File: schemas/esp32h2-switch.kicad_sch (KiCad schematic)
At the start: 21 parts, among them J1 Screw_Terminal_01x02, J2 Screw_Terminal_01x02, J3 Conn_01x15, J4 Conn_01x15, K1 SPDT, 5V 72R, 10A 250VAC, Q1 NPN, 40V, 500mA, U1 LM1117MP-3.3

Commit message: Fix nets due to checks
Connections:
- net L: no longer F1.1, J1.1 (Pin_1), J2.1 (Pin_1), K1.11, K1.14
- new net L_IN: F1.1, J1.1 (Pin_1), K1.11
- new net L_OUT: J2.1 (Pin_1), K1.14
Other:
- moved on the sheet: F1, J2, RV1
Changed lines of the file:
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@@
 	)
 	(junction
+		(at 86.36 71.12)
+		(diameter 0)
+		(color 0 0 0 0)
+	)
+	(junction
 		(at 87.63 118.11)
 		(diameter 0)
@@
 	)
 	(junction
-		(at 83.82 78.74)
+		(at 86.36 78.74)
 		(diameter 0)
 		(color 0 0 0 0)
@@
 	)
 	(junction
-		(at 83.82 71.12)
-		(diameter 0)
-		(color 0 0 0 0)
-	)
-	(junction
 		(at 99.06 118.11)
 		(diameter 0)
@@
 	(wire
 		(pts
-			(xy 99.06 118.11) (xy 114.3 118.11)
+			(xy 86.36 71.12) (xy 99.06 71.12)
 		)
 		(stroke
@@
 	(wire
 		(pts
-			(xy 83.82 71.12) (xy 99.06 71.12)
+			(xy 99.06 118.11) (xy 114.3 118.11)
 		)
 		(stroke
@@
 	(wire
 		(pts
-			(xy 68.58 71.12) (xy 72.39 71.12)
+			(xy 73.66 71.12) (xy 74.93 71.12)
 		)
 		(stroke
@@
 	(wire
 		(pts
-			(xy 182.88 128.27) (xy 186.69 128.27)
-		)
-		(stroke
-			(width 0)
-			(type default)
-		)
-	)
-	(wire
-		(pts
 			(xy 196.85 95.25) (xy 196.85 105.41)
 		)
@@
 	(wire
 		(pts
+			(xy 86.36 78.74) (xy 99.06 78.74)
+		)
+		(stroke
+			(width 0)
+			(type default)
+		)
+	)
+	(wire
+		(pts
 			(xy 72.39 118.11) (xy 87.63 118.11)
 		)
@@
 	(wire
 		(pts
-			(xy 80.01 71.12) (xy 83.82 71.12)
+			(xy 182.88 128.27) (xy 190.5 128.27)
+		)
+		(stroke
+			(width 0)
+			(type default)
+		)
+	)
+	(wire
+		(pts
+			(xy 82.55 71.12) (xy 86.36 71.12)
 		)
 		(stroke
@@
 	(wire
 		(pts
-			(xy 157.48 134.62) (xy 186.69 134.62)
+			(xy 157.48 134.62) (xy 190.5 134.62)
 		)
 		(stroke
@@
 	(wire
 		(pts
-			(xy 186.69 130.81) (xy 186.69 134.62)
+			(xy 190.5 130.81) (xy 190.5 134.62)
 		)
 		(stroke
@@
 	(wire
 		(pts
-			(xy 68.58 78.74) (xy 83.82 78.74)
+			(xy 73.66 78.74) (xy 86.36 78.74)
 		)
 		(stroke
@@
 	(wire
 		(pts
-			(xy 83.82 78.74) (xy 99.06 78.74)
-		)
-		(stroke
-			(width 0)
-			(type default)
-		)
-	)
-	(wire
-		(pts
 			(xy 99.06 118.11) (xy 99.06 116.84)
 		)
@@
 		)
 	)
-	(label "L"
-		(at 184.15 128.27 0)
+	(label "RELAY_COIL"
+		(at 184.15 115.57 0)
 		(effects
 			(font
@@
 		)
 	)
-	(label "RELAY_COIL"
-		(at 184.15 115.57 0)
+	(label "RELAY_CTRL"
+		(at 193.04 72.39 180)
 		(effects
 			(font
 				(size 1.27 1.27)
 			)
-			(justify left bottom)
+			(justify right bottom)
 		)
 	)
-	(label "RELAY_CTRL"
-		(at 193.04 72.39 180)
+	(label "L_OUT"
+		(at 184.15 128.27 0)
 		(effects
 			(font
 				(size 1.27 1.27)
 			)
-			(justify right bottom)
+			(justify left bottom)
 		)
 	)
 	(label "L"
-		(at 86.36 71.12 0)
+		(at 95.25 71.12 0)
 		(effects
 			(font
@@
 		(lib_name "Screw_Terminal_01x02_1")
 		(lib_id "Connector:Screw_Terminal_01x02")
-		(at 191.77 128.27 0)
+		(at 195.58 128.27 0)
 		(unit 1)
 		(exclude_from_sim no)
@@
 		(dnp no)
 		(property "Reference" "J2"
-			(at 191.77 133.604 0)
+			(at 195.58 133.604 0)
 			(effects
 				(font
@@
 		)
 		(property "Value" "Screw_Terminal_01x02"
-			(at 191.77 134.62 0)
+			(at 195.58 134.62 0)
 			(effects
 				(font
@@
 		)
 		(property "Footprint" "TerminalBlock_Phoenix:TerminalBlock_Phoenix_MKDS-1,5-2-5.08_1x02_P5.08mm_Horizontal"
-			(at 191.77 128.27 0)
+			(at 195.58 128.27 0)
 			(effects
 				(font
@@
 		)
 		(property "Datasheet" "~"
-			(at 191.77 128.27 0)
+			(at 195.58 128.27 0)
 			(effects
 				(font
@@
 		)
 		(property "Description" "Generic screw terminal, single row, 01x02, script generated (kicad-library-utils/schlib/autogen/connector/)"
-			(at 191.77 128.27 0)
+			(at 195.58 128.27 0)
 			(effects
 				(font
@@
 		(on_board yes)
 		(dnp no)
-		(fields_autoplaced yes)
 		(property "Reference" "#PWR012"
 			(at 161.29 125.73 0)
@@
 			)
 		)
-		(property "Value" "L"
-			(at 153.67 125.7299 90)
+		(property "Value" "L_IN"
+			(at 151.638 125.73 90)
 			(effects
 				(font
 					(size 1.27 1.27)
 				)
-				(justify left)
 			)
 		)
@@
 		(lib_name "Varistor_1")
 		(lib_id "Device:Varistor")
-		(at 83.82 74.93 0)
+		(at 86.36 74.93 0)
 		(unit 1)
 		(exclude_from_sim no)
@@
 		(fields_autoplaced yes)
 		(property "Reference" "RV1"
-			(at 86.36 73.8532 0)
+			(at 88.9 73.8532 0)
 			(effects
 				(font
@@
 		)
 		(property "Value" "275V"
-			(at 86.36 76.3932 0)
+			(at 88.9 76.3932 0)
 			(effects
 				(font
@@
 		)
 		(property "Footprint" "Varistor:RV_Disc_D9mm_W3.4mm_P5mm"
-			(at 82.042 74.93 90)
+			(at 84.582 74.93 90)
 			(effects
 				(font
@@
 		)
 		(property "Datasheet" "~"
-			(at 83.82 74.93 0)
+			(at 86.36 74.93 0)
 			(effects
 				(font
@@
 		)
 		(property "Description" "Voltage dependent resistor"
-			(at 83.82 74.93 0)
+			(at 86.36 74.93 0)
 			(effects
 				(font
@@
 		)
 		(property "Sim.Name" "kicad_builtin_varistor"
-			(at 83.82 74.93 0)
+			(at 86.36 74.93 0)
 			(effects
 				(font
@@
 		)
 		(property "Sim.Device" "SUBCKT"
-			(at 83.82 74.93 0)
+			(at 86.36 74.93 0)
 			(effects
 				(font
@@
 		)
 		(property "Sim.Pins" "1=A 2=B"
-			(at 83.82 74.93 0)
+			(at 86.36 74.93 0)
 			(effects
 				(font
@@
 		)
 		(property "Sim.Params" "threshold=1k"
-			(at 83.82 74.93 0)
+			(at 86.36 74.93 0)
 			(effects
 				(font
@@
 		)
 		(property "Sim.Library" "${KICAD9_SYMBOL_DIR}/Simulation_SPICE.sp"
-			(at 83.82 74.93 0)
+			(at 86.36 74.93 0)
 			(effects
 				(font
@@
 	(symbol
 		(lib_id "Device:Fuse")
-		(at 76.2 71.12 90)
+		(at 78.74 71.12 90)
 		(unit 1)
 		(exclude_from_sim no)
@@
 		(fields_autoplaced yes)
 		(property "Reference" "F1"
-			(at 76.2 64.77 90)
+			(at 78.74 64.77 90)
 			(effects
 				(font
@@
 		)
 		(property "Value" "T250mA 250V"
-			(at 76.2 67.31 90)
+			(at 78.74 67.31 90)
 			(effects
 				(font
@@
 		)
 		(property "Footprint" "Sivakov_FuseHolders_THT:FuseHolder_THT_5x20mm_PTF76_RM15mm"
-			(at 76.2 72.898 90)
+			(at 78.74 72.898 90)
 			(effects
 				(font
@@
 		)
 		(property "Datasheet" "~"
-			(at 76.2 71.12 0)
+			(at 78.74 71.12 0)
 			(effects
 				(font
@@
 		)
 		(property "Description" "Fuse"
-			(at 76.2 71.12 0)
+			(at 78.74 71.12 0)
 			(effects
 				(font
@@
 			)
 		)
-		(property "Value" "L"
+		(property "Value" "L_IN"
 			(at 59.69 71.1199 90)
 			(effects
@@
 	(symbol
 		(lib_id "power:+5V")
-		(at 68.58 78.74 90)
+		(at 73.66 78.74 90)
 		(unit 1)
 		(exclude_from_sim no)
@@
 		(fields_autoplaced yes)
 		(property "Reference" "#PWR06"
-			(at 72.39 78.74 0)
+			(at 77.47 78.74 0)
 			(effects
 				(font
@@
 		)
 		(property "Value" "N"
-			(at 64.77 78.7399 90)
+			(at 69.85 78.7399 90)
 			(effects
 				(font
@@
 		)
 		(property "Footprint" ""
-			(at 68.58 78.74 0)
+			(at 73.66 78.74 0)
 			(effects
 				(font
@@
 		)
 		(property "Datasheet" ""
-			(at 68.58 78.74 0)
+			(at 73.66 78.74 0)
 			(effects
 				(font
@@
 		)
 		(property "Description" "Power symbol creates a global label with name \"+5V\""
-			(at 68.58 78.74 0)
+			(at 73.66 78.74 0)
 			(effects
 				(font
@@
 	(symbol
 		(lib_id "power:+5V")
-		(at 68.58 71.12 90)
+		(at 73.66 71.12 90)
 		(unit 1)
 		(exclude_from_sim no)
@@
 		(on_board yes)
 		(dnp no)
-		(fields_autoplaced yes)
 		(property "Reference" "#PWR05"
-			(at 72.39 71.12 0)
+			(at 77.47 71.12 0)
 			(effects
 				(font
@@
 			)
 		)
-		(property "Value" "L"
-			(at 64.77 71.1199 90)
+		(property "Value" "L_IN"
+			(at 67.818 71.12 90)
 			(effects
 				(font
 					(size 1.27 1.27)
 				)
-				(justify left)
 			)
 		)
 		(property "Footprint" ""
-			(at 68.58 71.12 0)
+			(at 73.66 71.12 0)
 			(effects
 				(font
@@
 		)
 		(property "Datasheet" ""
-			(at 68.58 71.12 0)
+			(at 73.66 71.12 0)
 			(effects
 				(font
@@
 		)
 		(property "Description" "Power symbol creates a global label with name \"+5V\""
-			(at 68.58 71.12 0)
+			(at 73.66 71.12 0)
 			(effects
 				(font

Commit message: Better layout for hand soldering
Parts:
- Q1: footprint Package_TO_SOT_THT:TO-92_Inline -> Package_TO_SOT_THT:TO-92_Inline_Wide
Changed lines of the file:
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@@
 			)
 		)
-		(property "Footprint" "Package_TO_SOT_THT:TO-92_Inline"
+		(property "Footprint" "Package_TO_SOT_THT:TO-92_Inline_Wide"
 			(at 231.14 118.11 0)
 			(effects

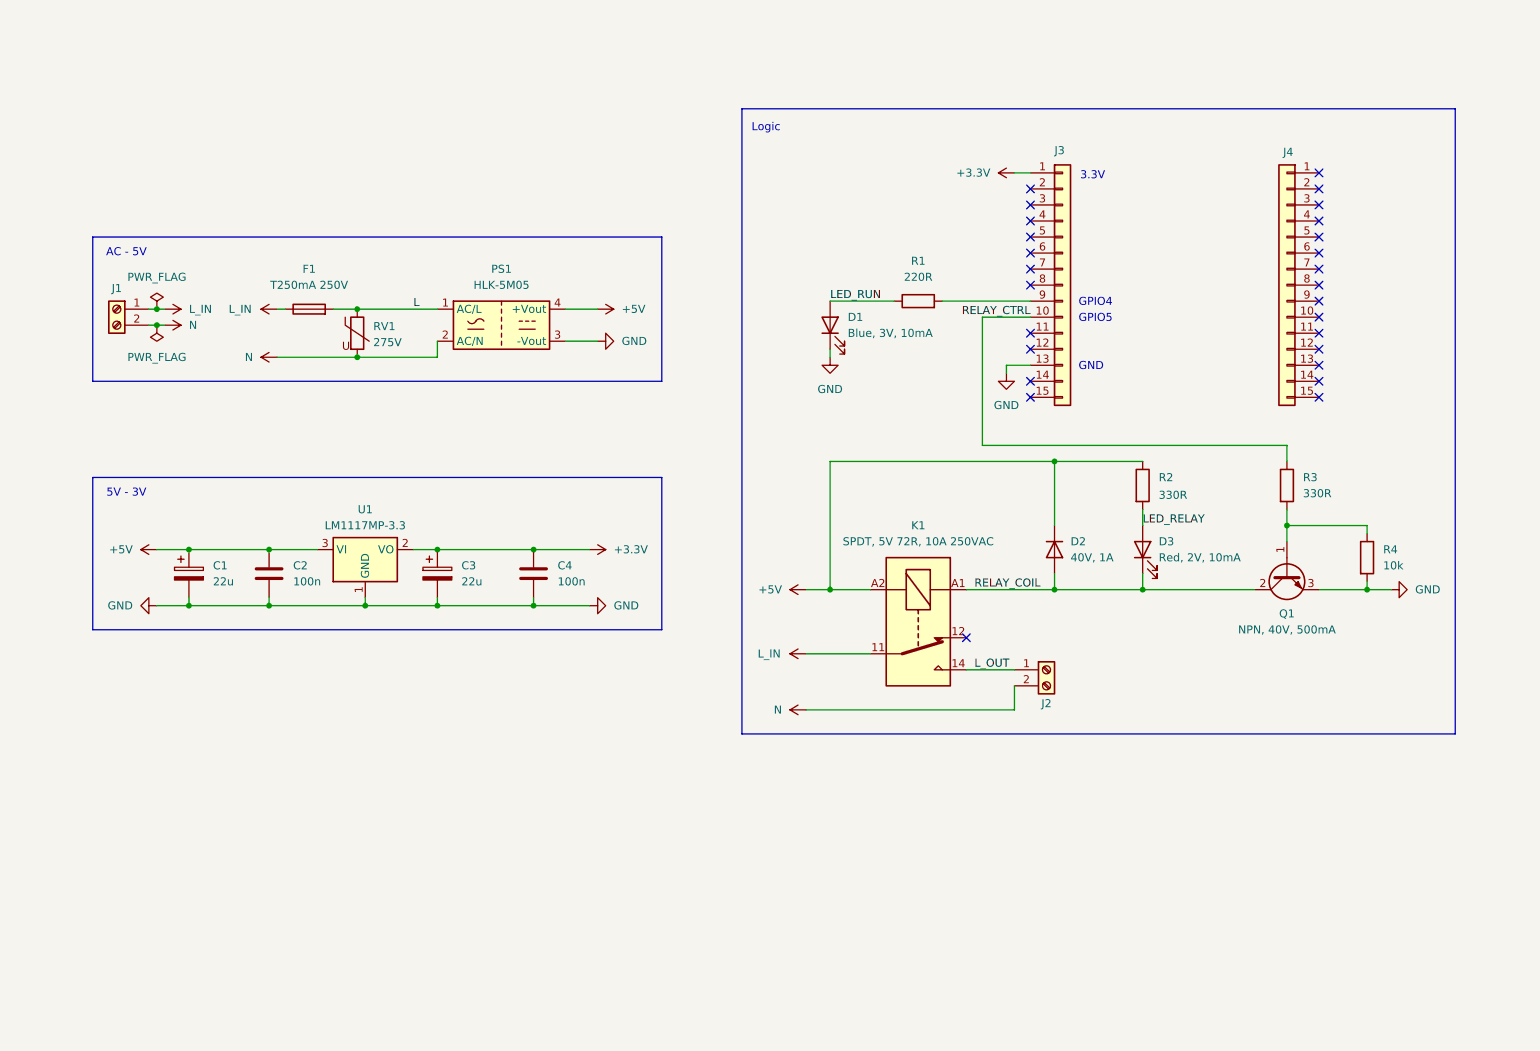
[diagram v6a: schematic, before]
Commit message: Fix footprints and improve layout for hand soldering
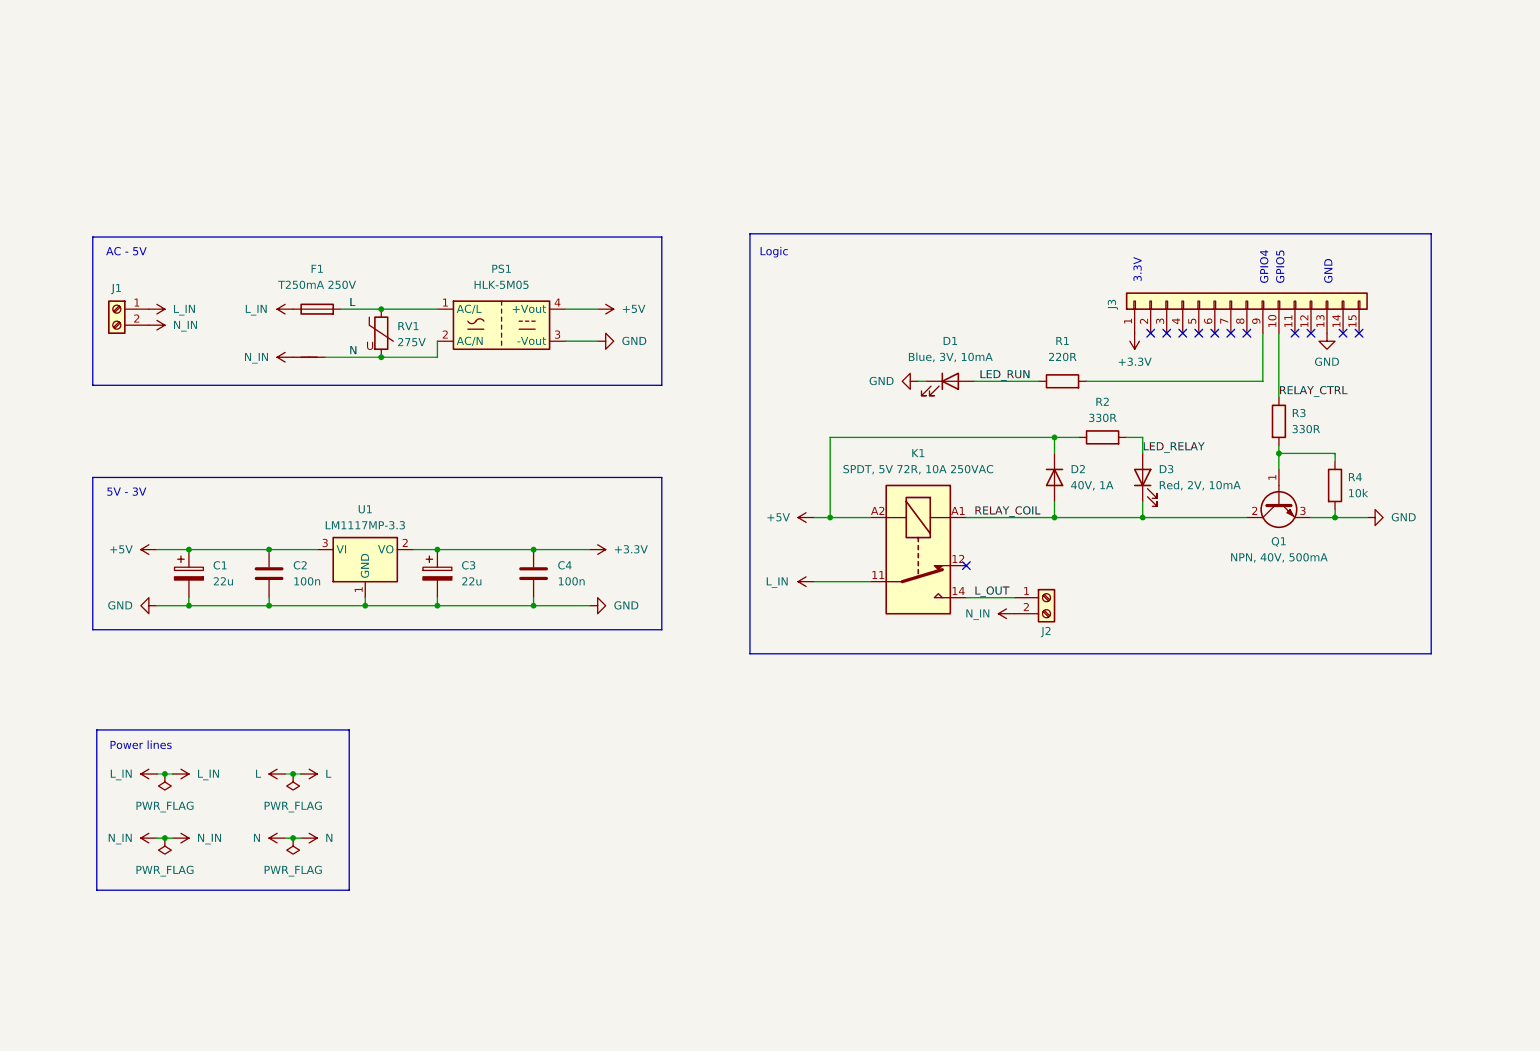
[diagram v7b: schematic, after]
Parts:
- removed J4: Conn_01x15, Connector_PinSocket_2.54mm:PinSocket_1x15_P2.54mm_Vertical, symbol Connector_Generic:Conn_01x15
- added NT1: NetTie_2, NetTie:NetTie-2_SMD_Pad2.0mm, symbol Device:NetTie_2
- C1, C3: footprint Sivakov_Capacitors_THT:CP_Radial_D5.0mm_P1.50mm -> KiCadX_Capacitors_THT:CP_Radial_D5.0mm_P1.50mm
- F1: footprint Sivakov_FuseHolders_THT:FuseHolder_THT_5x20mm_PTF76_RM15mm -> KiCadX_FuseHolders_THT:FuseHolder_THT_5x20mm_PTF76_RM15mm
- K1: footprint Sivakov_Relays_THT:Relay_SPDT_Relpol-RM51 -> KiCadX_Relays_THT:Relay_SPDT_Relpol-RM51
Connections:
- net N: now also NT1.2; no longer J1.2 (Pin_2), J2.2 (Pin_2)
- new net N_IN: J1.2 (Pin_2), J2.2 (Pin_2), NT1.1
- no-connect marks 27 -> 12
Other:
- note added: "Power lines"
- moved on the sheet: D1, D2, D3, F1, J2, J3, K1, Q1, R1, R3, R4, RV1

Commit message: Replace HLK block with SMPS
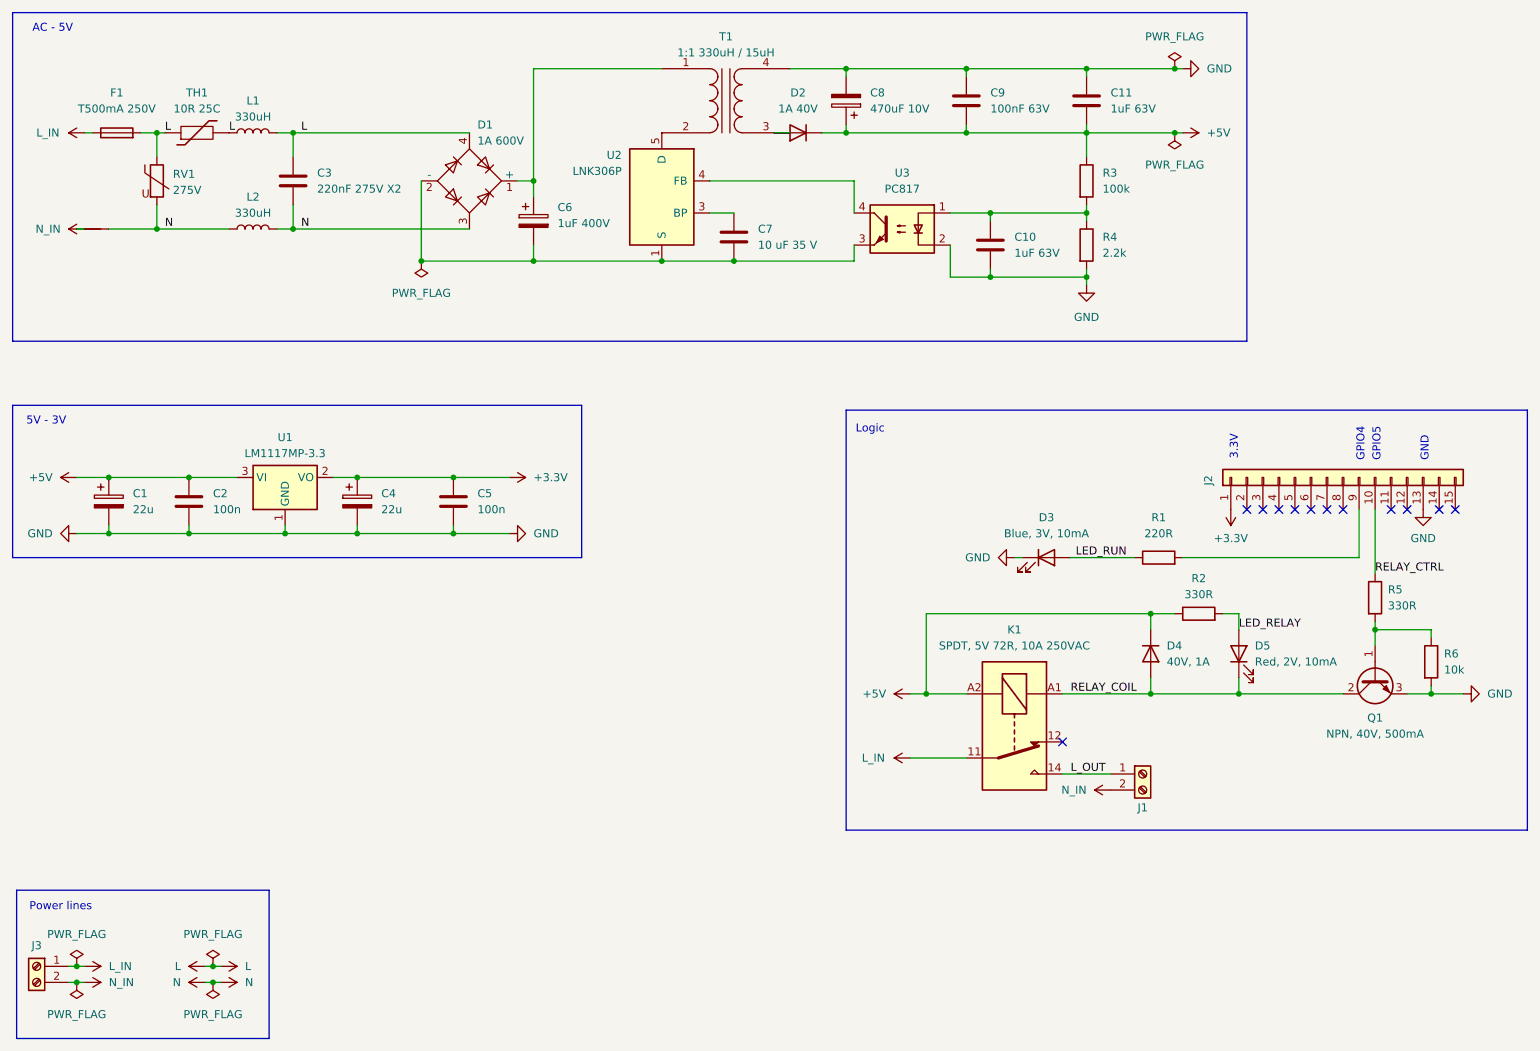
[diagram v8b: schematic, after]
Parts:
- removed J1: Screw_Terminal_01x02, TerminalBlock_Phoenix:TerminalBlock_Phoenix_MKDS-1,5-2-5.08_1x02_P5.08mm_Horizontal, symbol Connector:Screw_Terminal_01x02
- removed PS1: HLK-5M05, Converter_ACDC:Converter_ACDC_Hi-Link_HLK-5Mxx, symbol Converter_ACDC:HLK-5M05
- added C10, C11: 1uF 63V, symbol Device:C
- added C3: 220nF 275V X2, symbol Device:C
- added C6: 1uF 400V, symbol Device:C_Polarized
- added C7: 10 uF 35 V, symbol Device:C
- added C8: 470uF 10V, symbol Device:C_Polarized
- added C9: 100nF 63V, symbol Device:C
- added D1: 1A 600V, Diode_THT:Diode_Bridge_DIP-4_W7.62mm_P5.08mm, symbol Diode_Bridge:DF08M
- added D2: 1A 40V, symbol Device:D
- added J3: Screw_Terminal_01x02, TerminalBlock_Phoenix:TerminalBlock_Phoenix_MKDS-1,5-2-5.08_1x02_P5.08mm_Horizontal, symbol Connector:Screw_Terminal_01x02
- added L1, L2: 330uH, symbol Device:L
- added R3: 100k, symbol Device:R
- added R4: 2.2k, symbol Device:R
- added T1: 1:1 330uH / 15uH, symbol Device:Transformer_1P_1S
- added TH1: 10R 25C, symbol Device:Thermistor
- added U2: LNK306P, Package_DIP:PowerIntegrations_PDIP-8B, symbol Regulator_Switching:LNK306P
- added U3: PC817, Package_DIP:DIP-4_W7.62mm, symbol Isolator:PC817
- F1: value T250mA 250V -> T500mA 250V
- renumbered C3 to C4, C4 to C5, D1 to D3, D2 to D4, D3 to D5, J2 to J1, J3 to J2, R3 to R5, R4 to R6
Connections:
- net +5V: now also C11.2, C8.1, C9.2, D2.1 (K), R3.1
- net GND: now also C10.2, C11.1, C8.2, C9.1, R4.2, T1.4 (SB), U3.2
- net L: now also C3.1, D1.4, L1.1, L1.2, TH1.1, TH1.2
- net L_IN: now also J3.1 (Pin_1)
- net N: now also C3.2, D1.3, L2.1, L2.2
- net N_IN: now also J3.2 (Pin_2)
- new net: C7.1, U2.3 (BP)
- new net: C6.2, C7.2, D1.2 (-), U2.1 (S), U2.2 (S), U2.7 (S), U2.8 (S), U3.3
- new net: D2.2 (A), T1.3 (SA)
- new net: C6.1, D1.1 (+), T1.1 (AA)
- new net: C10.1, R3.2, R4.1, U3.1
- new net: U2.4 (FB), U3.4
- new net: T1.2 (AB), U2.5 (D)
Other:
- company: Sivakov Tech -> SIVAKOV.TECH
- moved on the sheet: C1, C2, C4, C5, D3, D4, D5, J1, J2, K1, Q1, R1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
